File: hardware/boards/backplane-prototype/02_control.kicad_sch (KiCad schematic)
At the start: 11 parts, among them J10 TC2030-IDC-NL SWD, U1 STM32C092GCU6

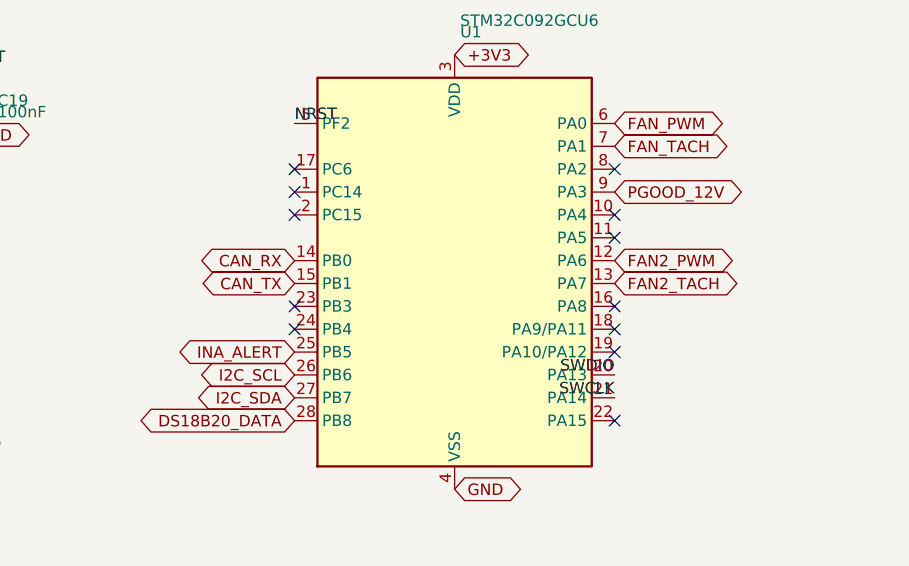
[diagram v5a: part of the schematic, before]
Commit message: hardware: reassign fan 2 and INA alert MCU pins
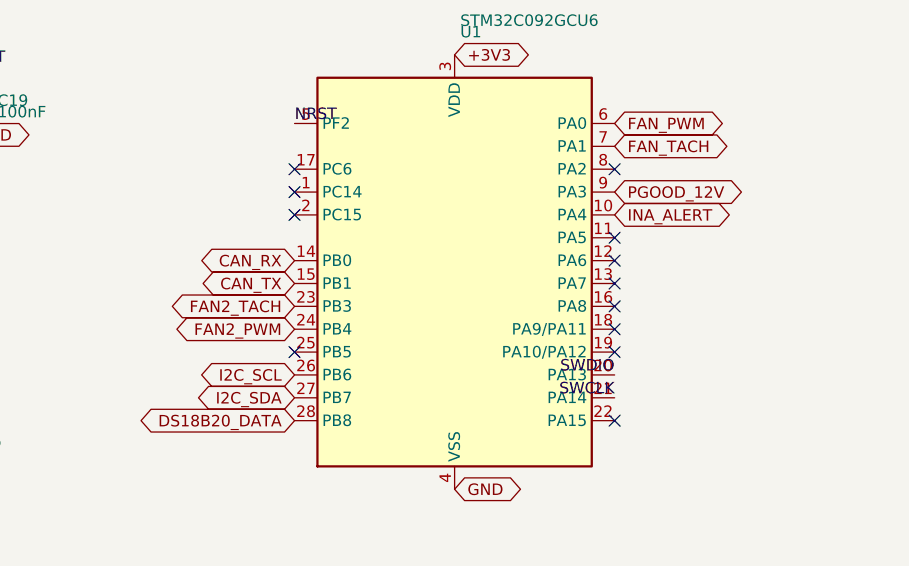
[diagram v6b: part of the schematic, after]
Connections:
- net FAN2_PWM: now also U1.24 (PB4); no longer U1.12 (PA6)
- net FAN2_TACH: now also U1.23 (PB3); no longer U1.13 (PA7)
- net INA_ALERT: now also U1.10 (PA4); no longer U1.25 (PB5)
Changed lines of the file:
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@@
 	)
 	(no_connect
-		(at 101.6 92.71)
-	)
-	(no_connect
-		(at 101.6 95.25)
+		(at 137.16 87.63)
+	)
+	(no_connect
+		(at 137.16 90.17)
 	)
 	(no_connect
@@
 	)
 	(no_connect
-		(at 137.16 82.55)
+		(at 101.6 97.79)
 	)
 	(no_connect
@@
 	(global_label "FAN2_TACH"
 		(shape bidirectional)
-		(at 137.16 90.17 0)
-		(effects
-			(font
-				(size 1.27 1.27)
-			)
-			(justify left)
-		)
-		(property "Intersheetrefs" "${INTERSHEET_REFS}"
-			(at 137.16 90.17 0)
+		(at 101.6 92.71 180)
+		(effects
+			(font
+				(size 1.27 1.27)
+			)
+			(justify right)
+		)
+		(property "Intersheetrefs" "${INTERSHEET_REFS}"
+			(at 101.6 92.71 0)
 			(hide yes)
 			(show_name no)
@@
 	(global_label "INA_ALERT"
 		(shape bidirectional)
-		(at 101.6 97.79 180)
+		(at 137.16 82.55 0)
+		(effects
+			(font
+				(size 1.27 1.27)
+			)
+			(justify left)
+		)
+		(property "Intersheetrefs" "${INTERSHEET_REFS}"
+			(at 137.16 82.55 0)
+			(hide yes)
+			(show_name no)
+			(do_not_autoplace no)
+			(effects
+				(font
+					(size 1.27 1.27)
+				)
+			)
+		)
+	)
+	(global_label "FAN2_PWM"
+		(shape bidirectional)
+		(at 101.6 95.25 180)
 		(effects
 			(font
@@
 		)
 		(property "Intersheetrefs" "${INTERSHEET_REFS}"
-			(at 101.6 97.79 0)
-			(hide yes)
-			(show_name no)
-			(do_not_autoplace no)
-			(effects
-				(font
-					(size 1.27 1.27)
-				)
-			)
-		)
-	)
-	(global_label "FAN2_PWM"
-		(shape bidirectional)
-		(at 137.16 87.63 0)
-		(effects
-			(font
-				(size 1.27 1.27)
-			)
-			(justify left)
-		)
-		(property "Intersheetrefs" "${INTERSHEET_REFS}"
-			(at 137.16 87.63 0)
-			(hide yes)
-			(show_name no)
+			(at 101.6 95.25 0)
+			(hide yes)
+			(show_name no)

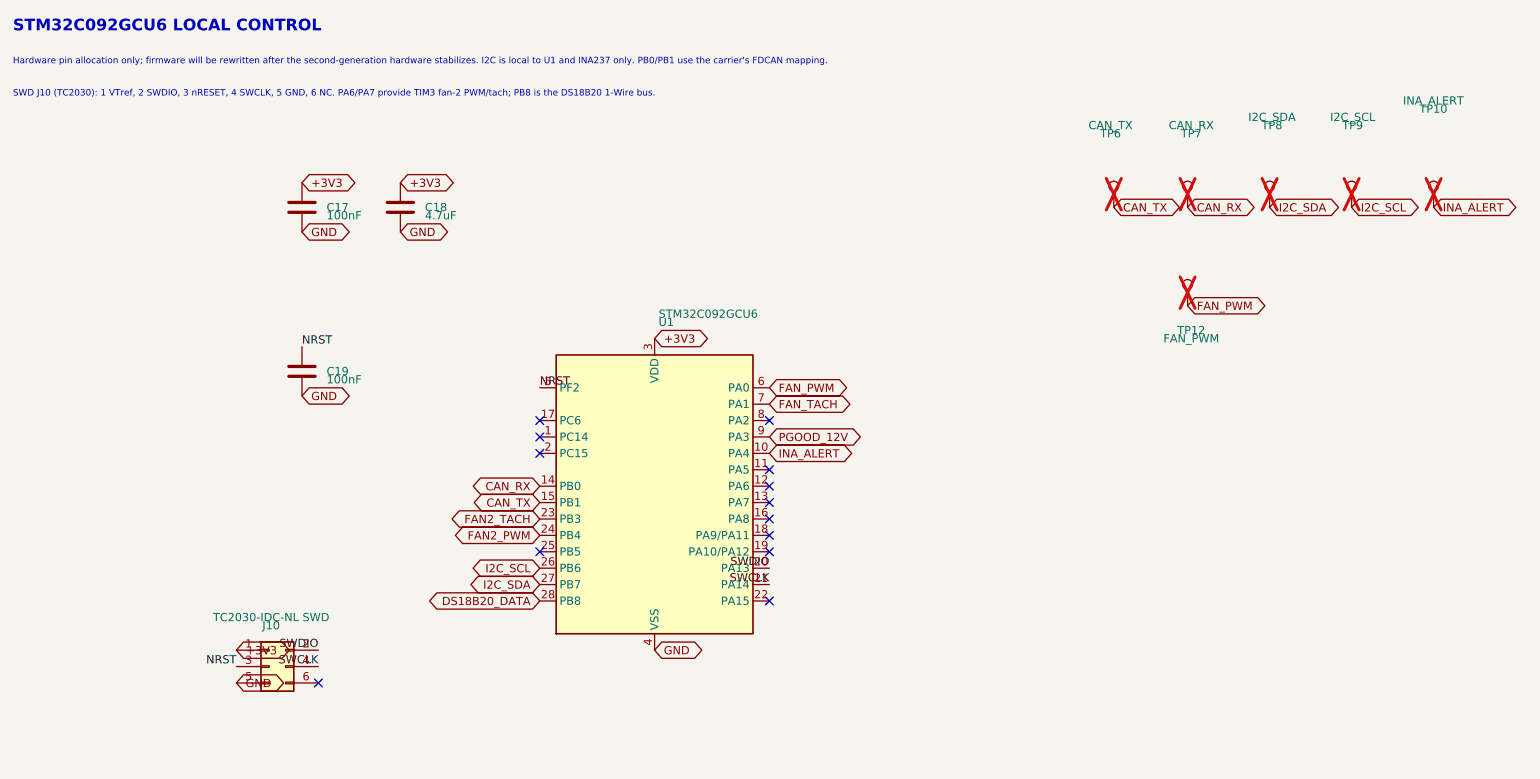
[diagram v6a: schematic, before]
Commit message: add backplane status NeoPixel
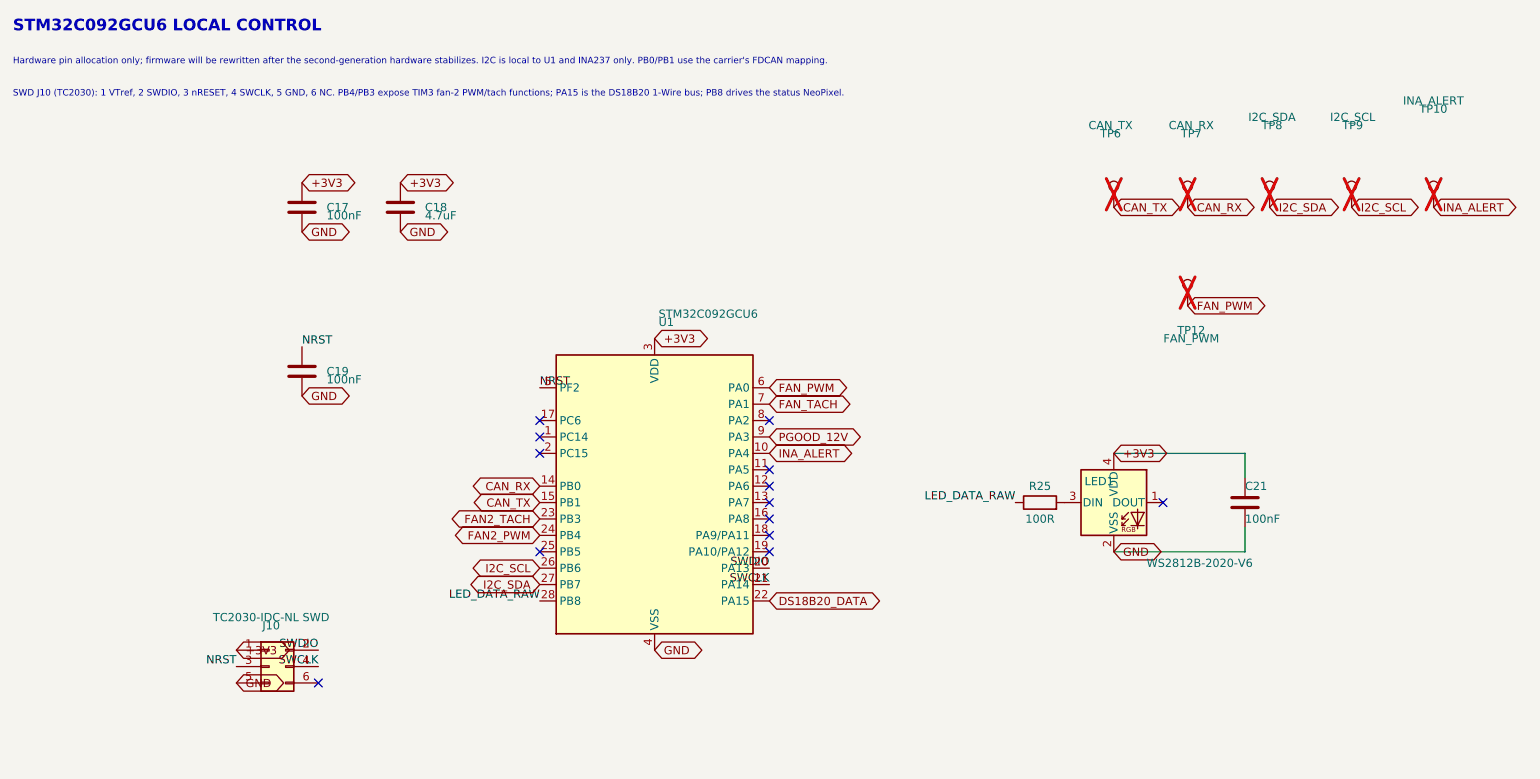
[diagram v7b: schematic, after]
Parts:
- added C21: 100nF, Capacitor_SMD:C_0603_1608Metric, symbol Device:C
- added LED1: WS2812B-2020-V6, LED_SMD:LED_WS2812B-2020_PLCC4_2.0x2.0mm, symbol LED:WS2812B-2020
- added R25: 100R, Resistor_SMD:R_0603_1608Metric, symbol Device:R
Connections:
- net +3V3: now also C21.1, LED1.4 (VDD)
- net DS18B20_DATA: now also U1.22 (PA15); no longer U1.28 (PB8)
- net GND: now also C21.2, LED1.2 (VSS)
- new net: LED1.3 (DIN), R25.2
- new net LED_DATA_RAW: R25.1, U1.28 (PB8)
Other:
- note added: "SWD J10 (TC2030): 1 VTref, 2 SWDIO, 3 nRESET, 4 SWCLK, 5 GND, 6 NC. PB4/PB3 expose TIM3 fan-2 PWM/tach functions; PA15 is the DS18B20 1-Wire bus; PB8 drives the status NeoPixel."
- note removed: "SWD J10 (TC2030): 1 VTref, 2 SWDIO, 3 nRESET, 4 SWCLK, 5 GND, 6 NC. PA6/PA7 provide TIM3 fan-2 PWM/tach; PB8 is the DS18B20 1-Wire bus."

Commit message: checkpoint before fan pin swap review
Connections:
- net FAN2_PWM: now also U1.6 (PA0); no longer U1.24 (PB4)
- net FAN2_TACH: now also U1.7 (PA1); no longer U1.23 (PB3)
- net FAN_PWM: now also U1.24 (PB4); no longer U1.6 (PA0)
- net FAN_TACH: now also U1.23 (PB3); no longer U1.7 (PA1)
